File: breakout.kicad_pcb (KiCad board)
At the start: 2 copper layers, 50 x 50 mm, 20 parts, among them P1 CONN_01X08, P2 SPEAKER, P3 ISO7816_SIMPLE, P4 CONN_01X04, P5 SMA_CONN, P6 CONN_01X08, Q1 Q_PMOS_GSD, Q2 Q_NMOS_GSD, U1 SPX3819, U2 ESP-12E

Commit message: More stuff.
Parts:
- removed P6: CONN_01X08, Pin_Headers:Pin_Header_Straight_1x08
- added J1: JACK_TRS_4PINS, Misc:PJ-320L, F.Cu at (184.8, 93.2)
- added P7: USB_A, Connect:USB_Micro-B_10103594-0001LF, F.Cu at (164.4, 53.8)
- C2, C4, P3, R1, R2, R3, R4, R5: moved to B.Cu
- C3: value 470 uF -> 100 uF; footprint Capacitors_ThroughHole:C_Radial_D8_L13_P3.8 -> Capacitors_Tantalum_SMD:TantalC_SizeB_EIA-3528_HandSoldering
- P4: value CONN_01X04 -> CONN_01X09; footprint Pin_Headers:Pin_Header_Straight_1x04 -> Pin_Headers:Pin_Header_Straight_1x09
- moved Q2 50.2 mm to (170.8, 60.1), turned to 180 degrees
- moved R6 49.3 mm to (166.8, 62.9), turned to 90 degrees
- moved P4 49.1 mm to (198.2, 51.8), turned to 270 degrees
- moved P1 46.1 mm to (198.1, 80.3)
- moved C3 40.7 mm to (152.7, 68.1), turned to 270 degrees
- moved U1 39.9 mm to (172.3, 53.3)
- moved P3 36.3 mm to (153.5, 95.6), turned to 0 degrees
- moved R5 29.7 mm to (185.1, 64.8), turned to 270 degrees
- moved R3 28.0 mm to (187.6, 64.8), turned to 270 degrees
- moved C2 27.1 mm to (182.6, 64.7), turned to 270 degrees
- moved P2 24.9 mm to (151.8, 95.8)
- moved R2 22.5 mm to (185.1, 59.2), turned to 90 degrees
- moved C4 22.0 mm to (174.2, 67.6), turned to 270 degrees
- moved R1 20.6 mm to (182.6, 59.2), turned to 90 degrees
- moved GSM1 14.6 mm to (162.4, 84.5), turned to 90 degrees
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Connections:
- net Net-(P1-Pad1) renamed /TX
- net Net-(P1-Pad2) renamed /RX
- net Net-(P1-Pad3) renamed /GPIO5
- net Net-(P1-Pad4) renamed /GPIO4
- net Net-(P1-Pad5) renamed /GPIO0
- net Net-(P1-Pad6) renamed /GPIO2
- GSM1 pad 19: (no net) -> GND
- GSM1 pad 20: Net-(GSM1-Pad20) -> /MIC+
- GSM1 pad 23: Net-(GSM1-Pad23) -> /EARL
- GSM1 pad 24: Net-(GSM1-Pad24) -> /EARR
- GSM1 pad 30: Net-(GSM1-Pad30) -> /GPIO14
- GSM1 pad 31: Net-(GSM1-Pad31) -> /GPIO12
- P4 pad 1: Net-(GSM1-Pad23) -> /REST
- P4 pad 2: Net-(GSM1-Pad24) -> /ADC
- P4 pad 3: GND -> /CH_PD
- P4 pad 4: Net-(GSM1-Pad20) -> /GPIO16
- R1 pad 2: Net-(P6-Pad3) -> /CH_PD
- R2 pad 2: Net-(P6-Pad1) -> /REST
- U2 pad 1: Net-(P6-Pad1) -> /REST
- U2 pad 2: Net-(P6-Pad2) -> /ADC
- U2 pad 3: Net-(P6-Pad3) -> /CH_PD
- U2 pad 4: Net-(P6-Pad4) -> /GPIO16
- U2 pad 5: Net-(GSM1-Pad30) -> /GPIO14
- U2 pad 6: Net-(GSM1-Pad31) -> /GPIO12
- U2 pad 7: Net-(P6-Pad7) -> /GPIO13
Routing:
- net /PWRCTL: track 0.00 -> 53.4 mm, vias 0 -> 1
- net /VBAT: track 0.00 -> 50.4 mm
- net /GPIO14: track 0.00 -> 38.4 mm, vias 0 -> 2
- net /GPIO2: track 0.00 -> 35.7 mm, vias 0 -> 1
- net /GPIO12: track 0.00 -> 35.3 mm, vias 0 -> 2
- net GND: track 0.00 -> 34.9 mm, vias 0 -> 2
- net /GPIO0: track 0.00 -> 32.1 mm, vias 0 -> 1
- net /MIC+: track 0.00 -> 31.8 mm
- net VCC: track 0.00 -> 29.6 mm
- net /3V3: track 0.00 -> 27.4 mm, vias 0 -> 1
- net Net-(C4-Pad2): track 0.00 -> 25.9 mm
- net Net-(GSM1-Pad26): track 0.00 -> 24.9 mm
- net Net-(GSM1-Pad27): track 0.00 -> 24.4 mm
- net Net-(GSM1-Pad35): track 0.00 -> 22.6 mm
- net /CH_PD: track 0.00 -> 22.0 mm
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- added copper zone on B.Cu, net GND
- added copper zone on F.Cu, net GND
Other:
- outline, holes or cut-outs redrawn
- net class Power: trace_width 0.8 -> 0.6
- board text added: "ADC"
- board text added: "CH_PD"
- board text added: "EARL"
- board text added: "EARR"
- board text added: "GND"
- board text added: "IO0"
- board text added: "IO12"
- board text added: "IO13"
- board text added: "IO14"
- board text added: "IO15"
- board text added: "IO16"
- board text added: "IO2"
- board text added: "IO4"
- board text added: "IO5"
- board text added: "MIC+"
- board text added: "REST"
- board text added: "RX"
- board text added: "TX"
- board text added: "VCC"

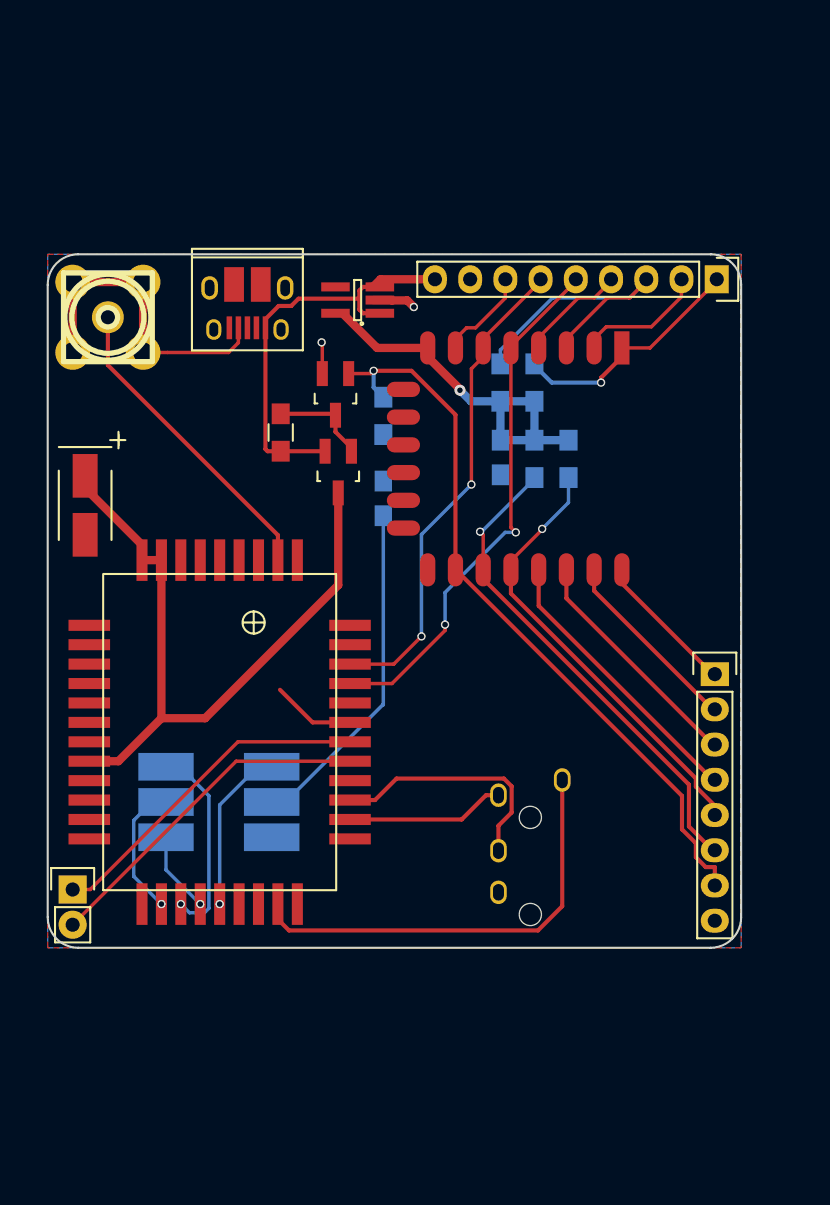
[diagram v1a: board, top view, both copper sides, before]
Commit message: Create image conversion script.
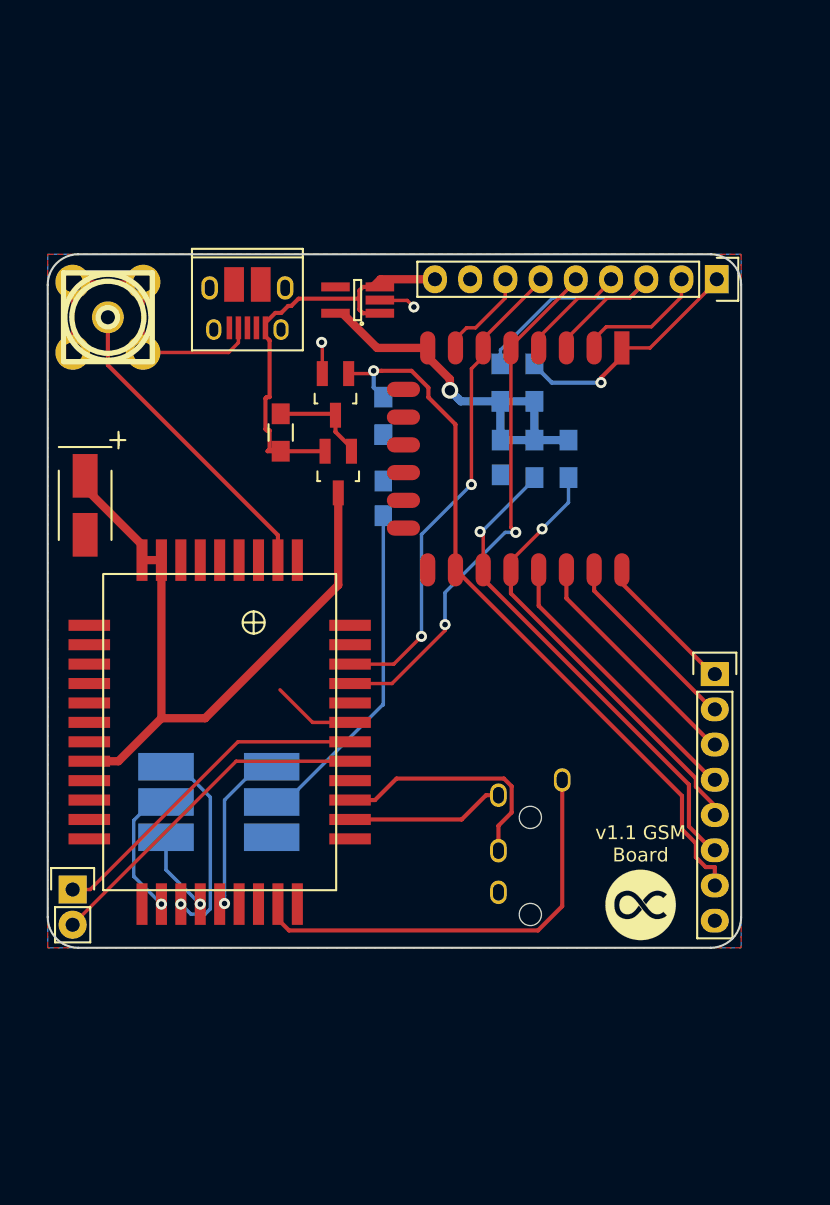
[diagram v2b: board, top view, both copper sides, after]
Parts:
- added G***: LOGO, Stochastic:Logo_5mm, F.Cu at (192.8, 96.9)
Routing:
- net VCC: track 29.6 -> 28.8 mm
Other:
- net class Default: via_dia 0.6 -> 0.8
- net class Power: via_dia 0.8 -> 1.2; via_drill 0.4 -> 0.75
- rule via_min_drill: 0.3 -> 0.4
- rule via_min_size: 0.4 -> 0.8
- board text added: "SPEAKER"
- board text added: "v1.1 GSM Board"

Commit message: Change version.
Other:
- board text added: "v0.1 GSM Board"
- board text removed: "v1.1 GSM Board"
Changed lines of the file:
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@@
     (effects (font (size 1 1) (thickness 0.25)) (justify right mirror))
   )
-  (gr_text "v1.1 GSM\nBoard\n" (at 192.75 92.51) (layer F.SilkS)
+  (gr_text "v0.1 GSM\nBoard\n" (at 192.75 92.51) (layer F.SilkS)
     (effects (font (size 1 1) (thickness 0.25)))
   )

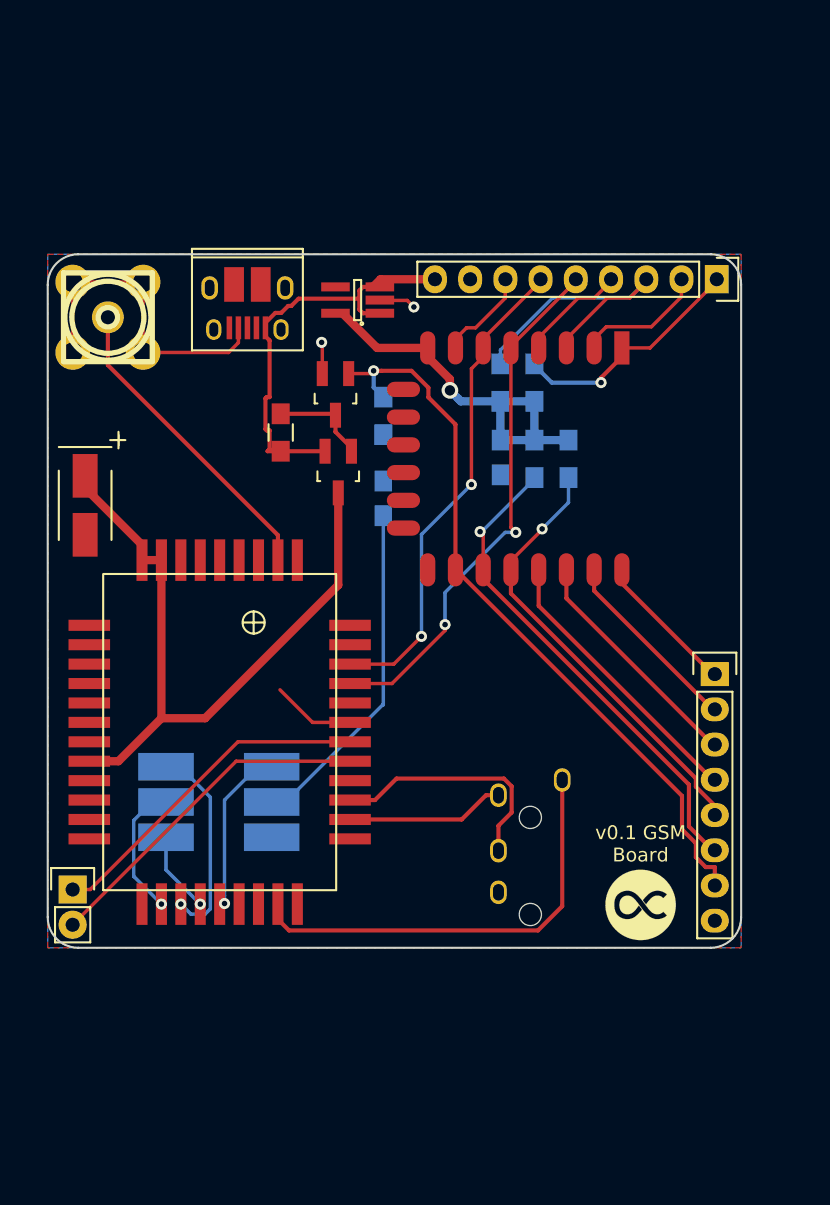
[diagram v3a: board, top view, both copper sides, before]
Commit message: Add labels to components.
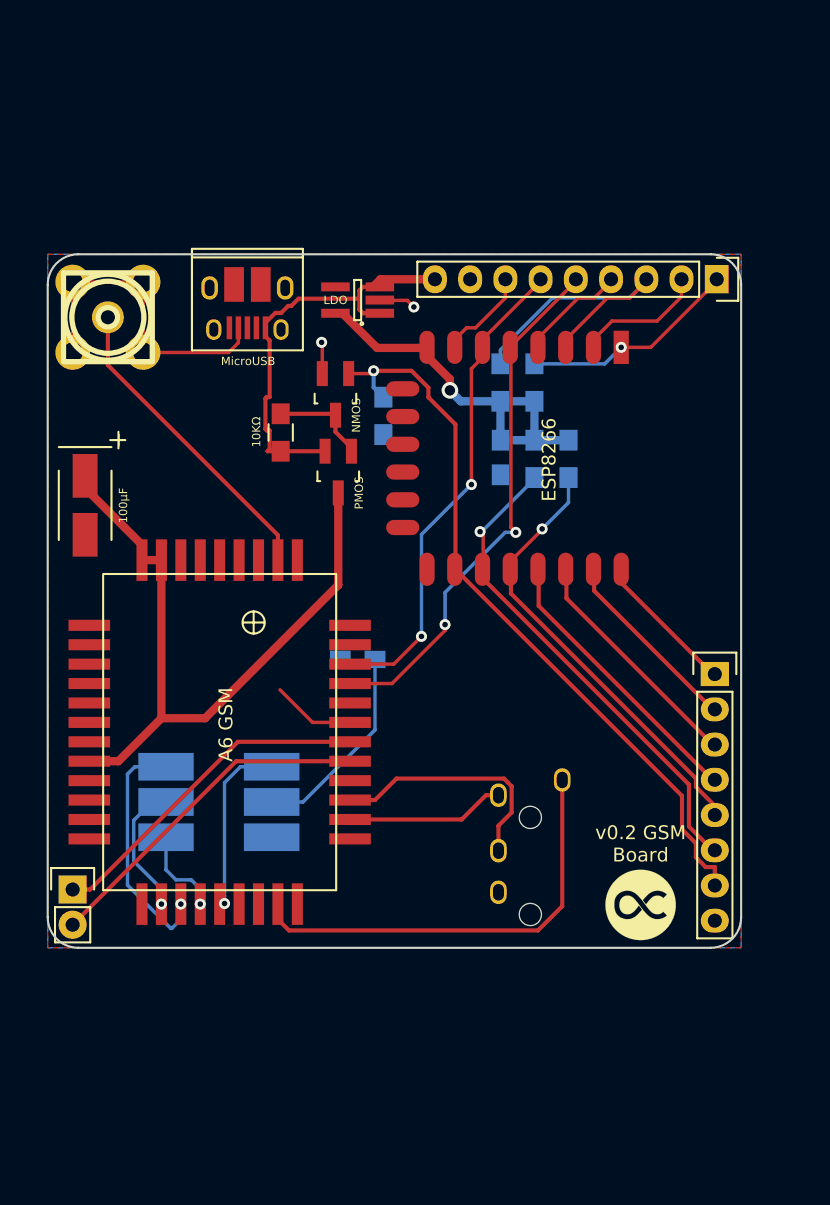
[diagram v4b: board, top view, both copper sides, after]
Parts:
- moved C4 11.8 mm to (172.3, 79.2), turned to 0 degrees
- moved U2 0.06 mm to (191.3, 56.7)
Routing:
- net Net-(C4-Pad2): track 25.9 -> 17.0 mm
- net Net-(GSM1-Pad15): track 14.7 -> 18.5 mm
- net /REST: track 17.5 -> 15.8 mm
- net Net-(GSM1-Pad17): track 11.9 -> 13.6 mm
- net Net-(GSM1-Pad16): track 5.84 -> 6.49 mm
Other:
- net class Default: trace_width 0.25 -> 0.3
- board text added: "0.1μF"
- board text added: "100μF"
- board text added: "10KΩ"
- board text added: "22μF"
- board text added: "A6 GSM"
- board text added: "ESP8266"
- board text added: "LDO"
- board text added: "MicroUSB"
- board text added: "NMOS"
- board text added: "PMOS"
- board text added: "SIM"
- board text added: "v0.2 GSM Board"
- board text removed: "v0.1 GSM Board"

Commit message: Add LED.
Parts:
- added D1: LED, LEDs:LED_0805, F.Cu at (158.4, 65.4)
- added R7: 150Ω, Resistors_SMD:R_0805_HandSoldering, F.Cu at (160.9, 65.4)
- moved G*** 0.20 mm to (192.9, 96.9)
- turned C3 to 90 degrees
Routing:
- net /VBAT: track 50.4 -> 54.4 mm
- net GND: track 34.9 -> 38.1 mm, vias 2 -> 3
- net Net-(GSM1-Pad15): track 18.5 -> 15.4 mm
- net Net-(D1-Pad1): track 0.00 -> 2.62 mm
- net Net-(C4-Pad2): track 17.0 -> 14.7 mm
- net Net-(GSM1-Pad35): track 22.6 -> 24.7 mm
- net Net-(GSM1-Pad17): track 13.6 -> 12.6 mm
- net Net-(GSM1-Pad14): track 9.74 -> 10.5 mm
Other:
- board text added: "150Ω"
- board text added: "LED"
- board text added: "v0.3 GSM Board"
- board text removed: "v0.2 GSM Board"

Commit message: Various updates.
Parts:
- P3: footprint smartcard:SIM_LIGHT -> Misc:SIM_115C_AC00_R
- moved P3 25.6 mm to (179.1, 97.0), turned to 90 degrees
- moved C4 14.0 mm to (160.2, 86.2), turned to 90 degrees
- moved G*** 0.14 mm to (192.8, 96.8)
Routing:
- net VCC: track 28.8 -> 51.9 mm, vias 0 -> 1
- net Net-(GSM1-Pad14): track 10.5 -> 26.7 mm
- net Net-(GSM1-Pad17): track 12.6 -> 19.4 mm
- net GND: track 38.1 -> 42.7 mm
- net Net-(C4-Pad2): track 14.7 -> 11.6 mm
- net Net-(GSM1-Pad16): track 6.49 -> 8.88 mm
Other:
- board text added: "v0.4 GSM Board"
- board text removed: "v0.3 GSM Board"

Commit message: Add microphone output.
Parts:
- added P6: CONN_01X02, Pin_Headers:Pin_Header_Straight_1x02, F.Cu at (183.0, 80.4)
- moved G*** 0.29 mm to (193.1, 96.9)
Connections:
- GSM1 pad 19: GND -> Net-(GSM1-Pad19)
- GSM1 pad 20: /MIC+ -> Net-(GSM1-Pad20)
- GSM1 pad 21: (no net) -> /MIC+
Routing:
- net Net-(GSM1-Pad19): track 0.00 -> 45.2 mm
- net Net-(GSM1-Pad20): track 0.00 -> 39.7 mm
- net /MIC+: track 31.8 -> 26.1 mm
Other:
- board text added: "MIC"
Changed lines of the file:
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@@
 (kicad_pcb (version 4) (host pcbnew 4.0.2+e4-6225~38~ubuntu15.10.1-stable)
   (general
-    (links 78)
+    (links 79)
     (no_connects 0)
     (area 147.900458 46.4 204.415 101.575001)
     (thickness 1.6)
-    (drawings 49)
-    (tracks 247)
+    (drawings 50)
+    (tracks 263)
     (zones 0)
-    (modules 24)
-    (nets 32)
+    (modules 25)
+    (nets 34)
   )
   (page A4)
@@
       (drillshape 0)
       (scaleselection 1)
-      (outputdirectory gerbers/))
+      (outputdirectory images/))
   )
   (net 0 "")
@@
   (net 30 /GPIO13)
   (net 31 "Net-(D1-Pad1)")
+  (net 32 "Net-(GSM1-Pad19)")
+  (net 33 "Net-(GSM1-Pad20)")
   (net_class Default "This is the default net class."
     (clearance 0.2)
@@
     (add_net "Net-(GSM1-Pad16)")
     (add_net "Net-(GSM1-Pad17)")
+    (add_net "Net-(GSM1-Pad19)")
+    (add_net "Net-(GSM1-Pad20)")
     (add_net "Net-(GSM1-Pad26)")
     (add_net "Net-(GSM1-Pad27)")
@@
       (net 1 GND))
     (pad 19 smd rect (at -12.4 2.8 180) (size 0.8 3) (layers F.Cu F.Paste F.Mask)
-      (net 1 GND))
+      (net 32 "Net-(GSM1-Pad19)"))
     (pad 20 smd rect (at -12.4 4.2 180) (size 0.8 3) (layers F.Cu F.Paste F.Mask)
+      (net 33 "Net-(GSM1-Pad20)"))
+    (pad 21 smd rect (at -12.4 5.6 180) (size 0.8 3) (layers F.Cu F.Paste F.Mask)
       (net 14 /MIC+))
-    (pad 21 smd rect (at -12.4 5.6 180) (size 0.8 3) (layers F.Cu F.Paste F.Mask))
     (pad 22 smd rect (at -7.7 9.4 270) (size 0.8 3) (layers F.Cu F.Paste F.Mask)
       (net 1 GND))
@@
       (net 1 GND))
   )
+  (module Pin_Headers:Pin_Header_Straight_1x02 (layer F.Cu)
+    (at 182.97 80.39)
+    (descr "Through hole pin header")
+    (tags "pin header")
+    (fp_text reference P6 (at 0 -5.1) (layer F.SilkS) hide
+      (effects (font (size 1 1) (thickness 0.15)))
+    )
+    (fp_text value CONN_01X02 (at 0 -3.1) (layer F.Fab) hide
+      (effects (font (size 1 1) (thickness 0.15)))
+    )
+    (fp_line (start 1.27 1.27) (end 1.27 3.81) (layer F.SilkS) (width 0.15))
+    (fp_line (start 1.55 -1.55) (end 1.55 0) (layer F.SilkS) (width 0.15))
+    (fp_line (start -1.75 -1.75) (end -1.75 4.3) (layer F.CrtYd) (width 0.05))
+    (fp_line (start 1.75 -1.75) (end 1.75 4.3) (layer F.CrtYd) (width 0.05))
+    (fp_line (start -1.75 -1.75) (end 1.75 -1.75) (layer F.CrtYd) (width 0.05))
+    (fp_line (start -1.75 4.3) (end 1.75 4.3) (layer F.CrtYd) (width 0.05))
+    (fp_line (start 1.27 1.27) (end -1.27 1.27) (layer F.SilkS) (width 0.15))
+    (fp_line (start -1.55 0) (end -1.55 -1.55) (layer F.SilkS) (width 0.15))
+    (fp_line (start -1.55 -1.55) (end 1.55 -1.55) (layer F.SilkS) (width 0.15))
+    (fp_line (start -1.27 1.27) (end -1.27 3.81) (layer F.SilkS) (width 0.15))
+    (fp_line (start -1.27 3.81) (end 1.27 3.81) (layer F.SilkS) (width 0.15))
+    (pad 1 thru_hole rect (at 0 0) (size 2.032 2.032) (drill 1.016) (layers *.Cu *.Mask F.SilkS)
+      (net 32 "Net-(GSM1-Pad19)"))
+    (pad 2 thru_hole oval (at 0 2.54) (size 2.032 2.032) (drill 1.016) (layers *.Cu *.Mask F.SilkS)
+      (net 33 "Net-(GSM1-Pad20)"))
+    (model Pin_Headers.3dshapes/Pin_Header_Straight_1x02.wrl
+      (at (xyz 0 -0.05 0))
+      (scale (xyz 1 1 1))
+      (rotate (xyz 0 0 90))
+    )
+  )
   (module Stochastic:Logo_5mm (layer F.Cu)
-    (at 192.85 96.81)
+    (at 193.13 96.9)
     (fp_text reference G*** (at 0 0) (layer F.SilkS) hide
       (effects (font (thickness 0.3)))
@@
       (xy -0.014256 -2.536727) (xy 0.042858 -2.536346)) (layer F.SilkS) (width 0.01))
   )
+  (gr_text MIC (at 180.43 81.66 270) (layer B.SilkS)
+    (effects (font (size 1 1) (thickness 0.25)) (justify mirror))
+  )
   (gr_text 150Ω (at 162.95 65.41 90) (layer F.SilkS)
     (effects (font (size 0.6 0.6) (thickness 0.15)))
@@
   (segment (start 170.75 62.80271) (end 171.9 63.95271) (width 0.3) (layer F.Cu) (net 13) (status 20))
   (segment (start 171.9 63.95271) (end 171.9 64.2) (width 0.3) (layer F.Cu) (net 13) (status 30))
-  (segment (start 187.1 87.9) (end 187.1 97.002002) (width 0.3) (layer F.Cu) (net 14) (status 10))
-  (segment (start 187.1 97.002002) (end 185.352001 98.750001) (width 0.3) (layer F.Cu) (net 14))
-  (segment (start 185.352001 98.750001) (end 167.400001 98.750001) (width 0.3) (layer F.Cu) (net 14))
-  (segment (start 166.6 97.95) (end 166.6 96.85) (width 0.3) (layer F.Cu) (net 14) (status 30))
-  (segment (start 167.400001 98.750001) (end 166.6 97.95) (width 0.3) (layer F.Cu) (net 14) (status 20))
+  (segment (start 168 96.85) (end 168.7 96.85) (width 0.3) (layer F.Cu) (net 14))
+  (segment (start 168.7 96.85) (end 169.05001 97.20001) (width 0.3) (layer F.Cu) (net 14))
+  (segment (start 169.05001 97.20001) (end 182.893507 97.20001) (width 0.3) (layer F.Cu) (net 14))
+  (segment (start 182.893507 97.20001) (end 187.1 92.993517) (width 0.3) (layer F.Cu) (net 14))
+  (segment (start 187.1 92.993517) (end 187.1 89.05) (width 0.3) (layer F.Cu) (net 14))
+  (segment (start 187.1 89.05) (end 187.1 87.9) (width 0.3) (layer F.Cu) (net 14))
   (segment (start 182.5 89) (end 181.6 89) (width 0.3) (layer F.Cu) (net 15) (status 10))
   (segment (start 181.6 89) (end 179.85 90.75) (width 0.3) (layer F.Cu) (net 15))
@@
   (segment (start 160.95 64.06) (end 158.75098 64.06) (width 0.3) (layer F.Cu) (net 31))
   (segment (start 158.75098 64.06) (end 158.45 64.36098) (width 0.3) (layer F.Cu) (net 31))
+  (segment (start 182.97 80.39) (end 184.286 80.39) (width 0.3) (layer F.Cu) (net 32))
+  (segment (start 184.286 80.39) (end 188.55002 84.65402) (width 0.3) (layer F.Cu) (net 32))
+  (segment (start 188.55002 84.65402) (end 188.55002 96.259102) (width 0.3) (layer F.Cu) (net 32))
+  (segment (start 188.55002 96.259102) (end 185.559111 99.250011) (width 0.3) (layer F.Cu) (net 32))
+  (segment (start 185.559111 99.250011) (end 166.500011 99.250011) (width 0.3) (layer F.Cu) (net 32))
+  (segment (start 165.2 97.95) (end 165.2 96.85) (width 0.3) (layer F.Cu) (net 32))
+  (segment (start 166.500011 99.250011) (end 165.2 97.95) (width 0.3) (layer F.Cu) (net 32))
+  (segment (start 182.97 82.93) (end 183.985999 83.945999) (width 0.3) (layer F.Cu) (net 33))
+  (segment (start 183.985999 83.945999) (end 184.739516 83.945999) (width 0.3) (layer F.Cu) (net 33))
+  (segment (start 184.739516 83.945999) (end 188.05001 87.256493) (width 0.3) (layer F.Cu) (net 33))
+  (segment (start 188.05001 87.256493) (end 188.05001 96.051992) (width 0.3) (layer F.Cu) (net 33))
+  (segment (start 188.05001 96.051992) (end 185.352001 98.750001) (width 0.3) (layer F.Cu) (net 33))
+  (segment (start 185.352001 98.750001) (end 167.400001 98.750001) (width 0.3) (layer F.Cu) (net 33))
+  (segment (start 167.400001 98.750001) (end 166.6 97.95) (width 0.3) (layer F.Cu) (net 33))
+  (segment (start 166.6 97.95) (end 166.6 96.85) (width 0.3) (layer F.Cu) (net 33))
   (zone (net 0) (net_name "") (layer F.Cu) (hatch full 0.508)
     (connect_pads (clearance 0.508))
